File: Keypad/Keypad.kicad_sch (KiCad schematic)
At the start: 15 parts, among them J1 addon_conn, SW1 TL1240GQ1JCLR, SW2 TL1240GQ1JCLR, SW3 TL1240GQ1JCLR, SW4 TL1240GQ1JCLR, SW5 TL1240GQ1JCLR, SW6 TL1240GQ1JCLR

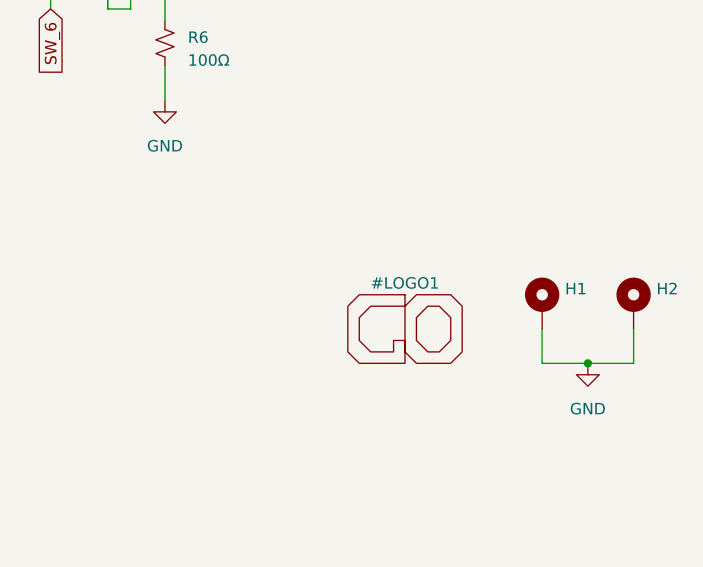
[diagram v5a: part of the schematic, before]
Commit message: Fixes logo reference in keypad schematics
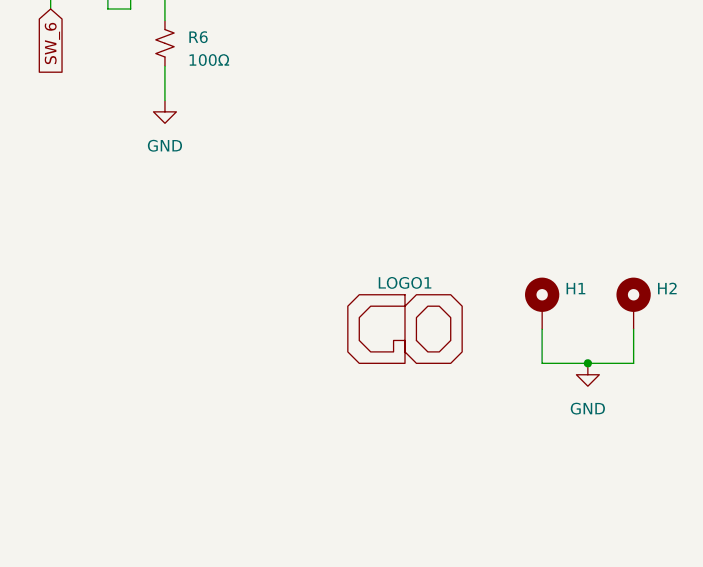
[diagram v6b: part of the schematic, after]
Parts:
- added LOGO1: (no value), symbol GameOver:GameOver_logo
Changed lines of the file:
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@@
   (symbol (lib_id "GameOver:GameOver_logo") (at 251.46 144.78 0) (unit 1)
     (in_bom no) (on_board yes) (fields_autoplaced)
-    (property "Reference" "#LOGO1" (id 0) (at 251.46 139.7 0)
-      (effects (font (size 1.27 1.27)))
-    )
-    (property "Value" "GameOver_logo" (id 1) (at 251.46 151.13 0)
-      (effects (font (size 1.27 1.27)) hide)
-    )
-    (property "Footprint" "GameOver:logo_fcu" (id 2) (at 251.46 144.78 0)
+    (property "Reference" "LOGO1" (id 0) (at 251.46 139.7 0)
+      (effects (font (size 1.27 1.27)))
+    )
+    (property "Value" "" (id 1) (at 251.46 151.13 0)
+      (effects (font (size 1.27 1.27)) hide)
+    )
+    (property "Footprint" "" (id 2) (at 251.46 144.78 0)
       (effects (font (size 1.27 1.27)) hide)
     )
@@
       (reference "#FLG02") (unit 1) (value "PWR_FLAG") (footprint "")
     )
-    (path "/a720fc4e-11cc-40fc-995d-9cf7d6347fff"
-      (reference "#LOGO1") (unit 1) (value "GameOver_logo") (footprint "GameOver:logo_fcu")
-    )
     (path "/f9e04c50-278a-4d44-a909-5802b74c4f31"
       (reference "#PWR01") (unit 1) (value "+3V3") (footprint "")
@@
       (reference "J1") (unit 1) (value "addon_conn") (footprint "GameOver:Addon_conn_TXGA_FFC05036-24SBD113W5M_1x24_P0.50mm_Horizontal")
     )
+    (path "/a720fc4e-11cc-40fc-995d-9cf7d6347fff"
+      (reference "LOGO1") (unit 1) (value "GameOver_logo") (footprint "GameOver:logo_fcu")
+    )
     (path "/c565d91c-47ce-4243-8169-b3049a31f847"

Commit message: Updates logo in the keypad schematics
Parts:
- LOGO1: value (none) -> GameOver_logo; footprint (none) -> GameOver:logo_fcu
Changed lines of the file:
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@@
       (effects (font (size 1.27 1.27)))
     )
-    (property "Value" "" (id 1) (at 251.46 151.13 0)
+    (property "Value" "GameOver_logo" (id 1) (at 251.46 151.13 0)
       (effects (font (size 1.27 1.27)) hide)
     )
-    (property "Footprint" "" (id 2) (at 251.46 144.78 0)
+    (property "Footprint" "GameOver:logo_fcu" (id 2) (at 251.46 144.78 0)
       (effects (font (size 1.27 1.27)) hide)
     )

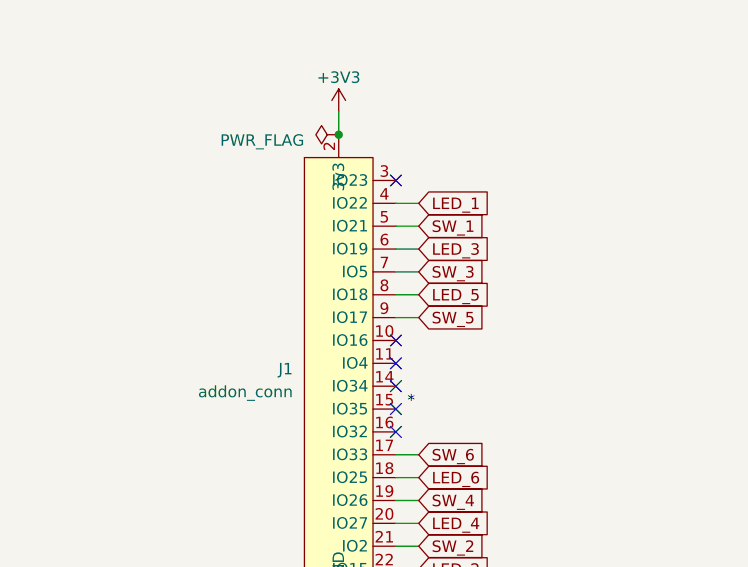
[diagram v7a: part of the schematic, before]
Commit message: Updates all add-on boards with fix introduced in 692041
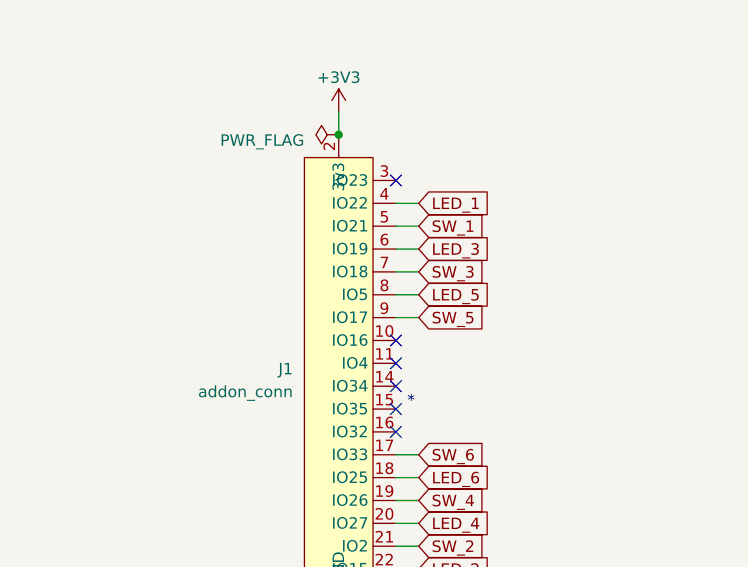
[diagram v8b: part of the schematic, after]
